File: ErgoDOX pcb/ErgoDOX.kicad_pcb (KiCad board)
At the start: 2 copper layers, 182.8 x 158.9 mm, 65 parts, among them J1 USB, J2 3.5mm, J3 JMP, J4 JMP, SW0:10 SW0:3, SW0:11 SW0:2, SW0:12 SW0:1, SW0:7 SW0:6, SW0:8 SW0:5, SW0:9 SW0:4, SW1:10 SW1:3, SW1:11 SW1:2, SW1:12 SW1:1, SW1:13 SW1:0, SW1:9 SW1:4, SW2:10 SW2:3, SW2:11 SW2:2, SW2:12 SW2:1, SW2:13 SW2:0, SW2:7 SW2:6, SW2:8 SW2:5, SW2:9 SW2:4, SW3:10 SW3:3, SW3:11 SW3:2, SW3:12 SW3:1, SW3:13 SW3:0, SW3:8 SW3:5, SW3:9 SW3:4, SW4:10 SW4:3, SW4:11 SW4:2, SW4:12 SW4:1, SW4:13 SW4:0, SW4:7 SW4:6, SW4:8 SW4:5, SW4:9 SW4:4, SW5:10 SW5:3, SW5:11 SW5:2, SW5:12 SW5:1, SW5:13 SW5:0, SW5:7 SW5:6, SW5:8 SW5:5, SW5:9 SW5:4, U1 TEENSY2.0, U2 MCP23018

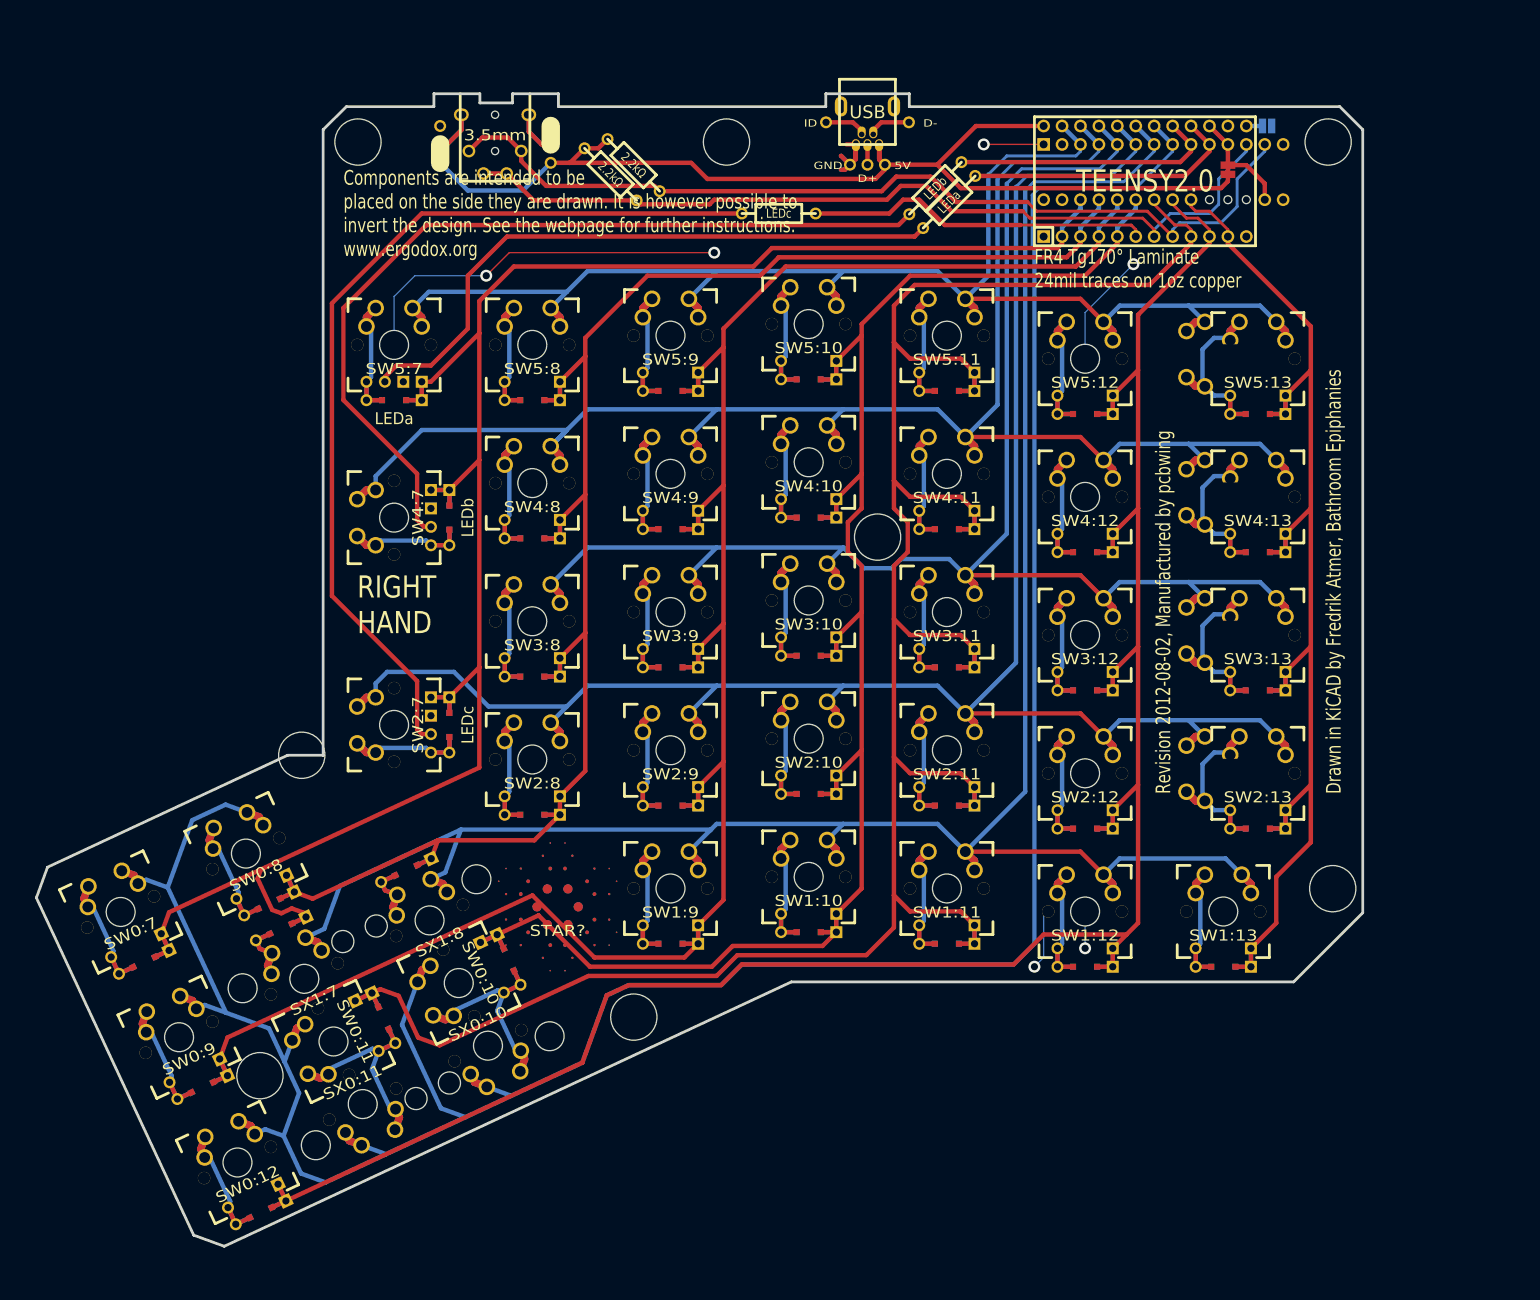
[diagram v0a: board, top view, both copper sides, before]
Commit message: アウトライン付きのスイッチに変更
いらないファイルを削除

名称変更
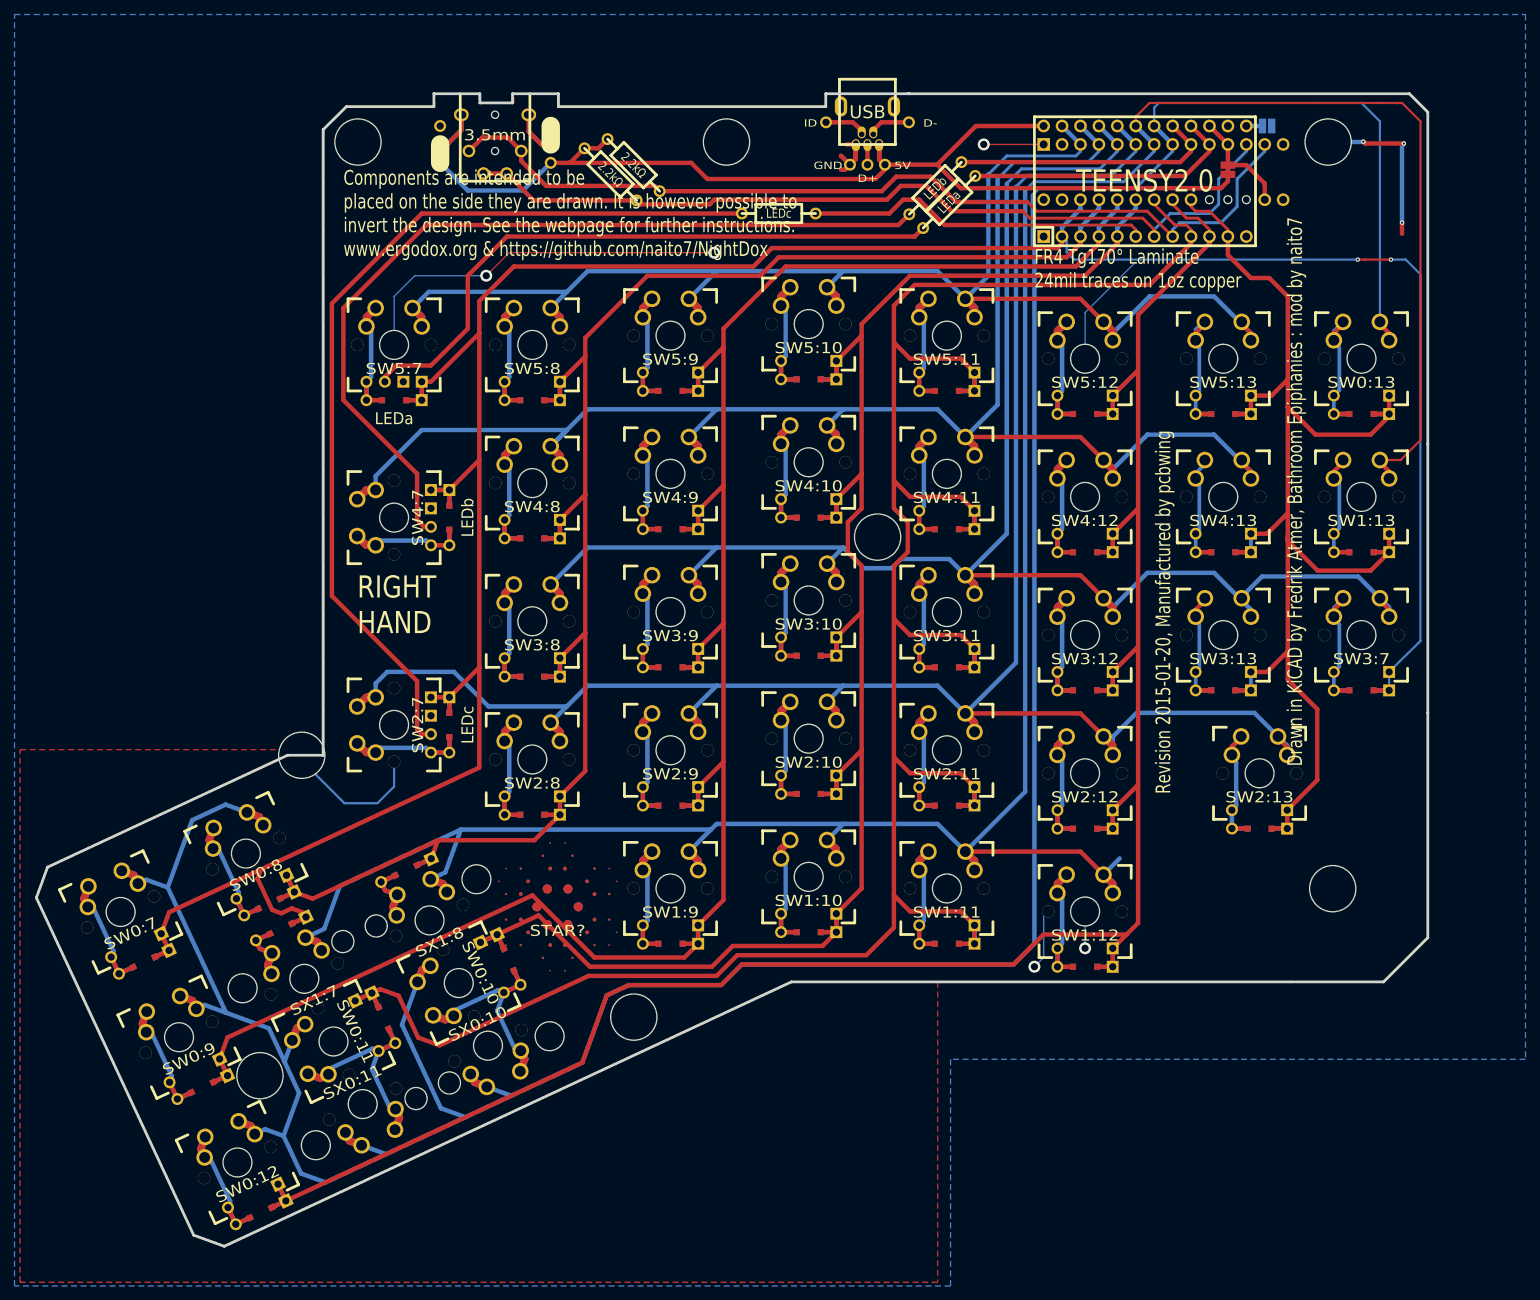
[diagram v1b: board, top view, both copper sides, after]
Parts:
- added SW0:13: SW0:0, MX_FLIP_DIODE_WITH_OUTLINE, F.Cu at (205.7, 67.0)
- added SW3:7: SW3:6, MX_FLIP_DIODE_WITH_OUTLINE, F.Cu at (205.7, 105.1)
- SW1:13: footprint MX_FLIP_DIODE -> MX_FLIP_DIODE_WITH_OUTLINE
- SW2:13, SW3:13, SW4:13, SW5:13: footprint MX_FLIP_XX -> MX_FLIP_DIODE_WITH_OUTLINE
- moved SW1:13 60.2 mm to (205.7, 86.1)
- moved SW2:13 5.00 mm to (191.7, 124.2)
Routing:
- net /COL6: track 259.5 -> 371.1 mm, vias 0 -> 2
- net /ROW1: track 318.2 -> 390.4 mm
- net /ROW0: track 404.2 -> 473.0 mm
- net GND: track 104.3 -> 147.7 mm, vias 6 -> 8
- net N-0000061: track 31.2 -> 13.6 mm
- net N-0000050: track 0.00 -> 16.9 mm
- net N-0000051: track 0.00 -> 16.9 mm
- net N-0000062: track 31.2 -> 16.7 mm
- net N-0000033: track 31.2 -> 16.8 mm
- net N-0000060: track 31.2 -> 16.8 mm
- net /ROW4: track 259.2 -> 245.3 mm
- net /ROW5: track 226.9 -> 214.0 mm
- net /ROW3: track 240.5 -> 251.5 mm
- net /ROW2: track 297.1 -> 290.1 mm
- net N-0000034: track 19.4 -> 13.9 mm
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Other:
- board size 182.8 x 158.9 mm -> 191.8 x 158.9 mm
- board text added: "Components are intended to be placed on the side they are drawn. It is however possible to invert the design. See the webpage for further instructions. www.ergodox.org & https://github.com/naito7/NightDox"
- board text added: "Design by Dominic Beauchamp, based on the Key64 by Nestor A. Diaz : mod by naito7"
- board text added: "Drawn in KiCAD by Fredrik Atmer, Bathroom Epiphanies : mod by naito7"
- board text added: "Night Dox"
- board text added: "Revision 2015-01-20, Manufactured by pcbwing"
- board text removed: "Components are intended to be placed on the side they are drawn. It is however possible to invert the design. See the webpage for further instructions. www.ergodox.org"
- board text removed: "Design by Dominic Beauchamp, based on the Key64 by Nestor A. Diaz"
- board text removed: "Drawn in KiCAD by Fredrik Atmer, Bathroom Epiphanies"
- board text removed: "ErgoDox"
- board text removed: "Revision 2012-08-02, Manufactured by pcbwing"
